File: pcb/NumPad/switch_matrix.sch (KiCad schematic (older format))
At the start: 49 parts, among them SW1 +, SW10 ,, SW11 *, SW12 9, SW13 6, SW14 3, SW15 ., SW16 /, SW17 FN2, SW18 FN1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

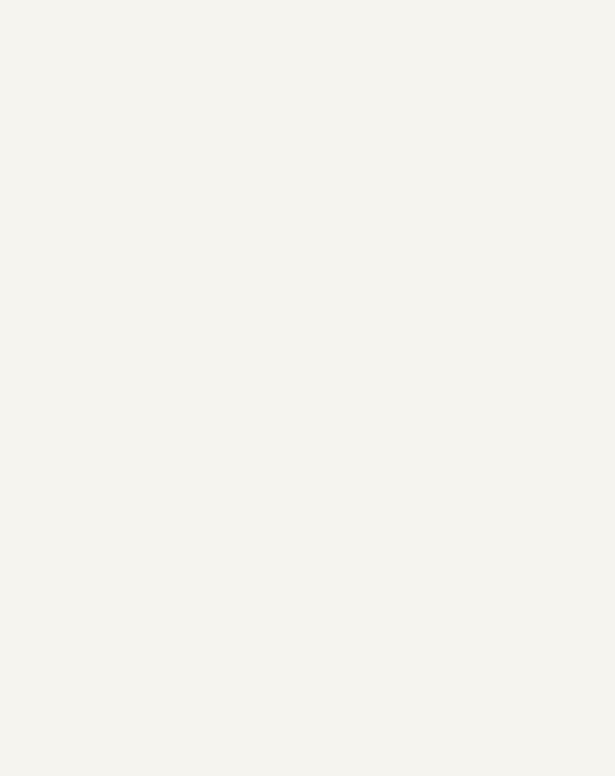
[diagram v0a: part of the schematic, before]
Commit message: started Numpad Layout
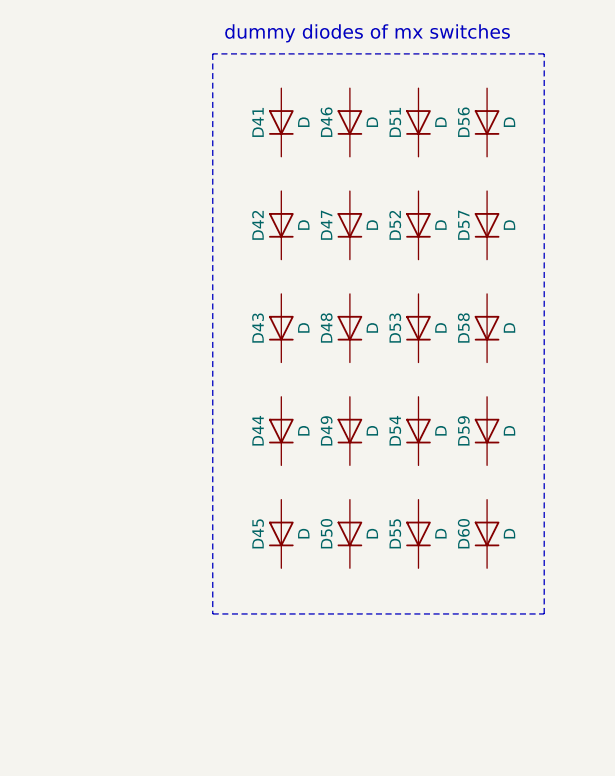
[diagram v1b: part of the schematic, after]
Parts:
- added D41, D42, D43, D44, D45, D46, D47, D48, D49, D50, D51, D52, D53, D54, D55, D56, D57, D58, D59, D60: D, footprints:CHERRY_MX_DIODE, symbol D
- D1, D10, D11, D12, D13, D14, D15, D16, D17, D18, D19, D2, D20, D3, D4, D5, D6, D7, D8, D9: footprint Diodes_SMD:D_SOD-523 -> Diodes_SMD:D_SOD-323_HandSoldering
- SW3: footprint footprints:CHERRY_PCB_150H -> footprints:CHERRY_PCB_100H
- SW4: footprint footprints:CHERRY_PCB_175H -> footprints:CHERRY_PCB_100H
- SW5: footprint footprints:CHERRY_PCB_125H -> footprints:CHERRY_PCB_100H
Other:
- note added: "dummy diodes of mx switches"

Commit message: changes in Numpad
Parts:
- removed D48, D53: D, footprints:CHERRY_MX_DIODE, symbol D
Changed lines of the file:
@@
-$EndComp
-$Comp
-L D D48
-U 1 1 5ABC28EE
-P 11250 5250
-F 0 "D48" H 11250 5350 50  0000 C CNN
-F 1 "D" H 11250 5150 50  0000 C CNN
-F 2 "footprints:CHERRY_MX_DIODE" H 11250 5250 50  0001 C CNN
-F 3 "" H 11250 5250 50  0001 C CNN
-	1    11250 5250
-	0    -1   -1   0
-$EndComp
-$Comp
-L D D53
-U 1 1 5ABC29B7
-P 11550 5250
-F 0 "D53" H 11550 5350 50  0000 C CNN
-F 1 "D" H 11550 5150 50  0000 C CNN
-F 2 "footprints:CHERRY_MX_DIODE" H 11550 5250 50  0001 C CNN
-F 3 "" H 11550 5250 50  0001 C CNN
-	1    11550 5250
-	0    -1   -1   0
 $EndComp
 $Comp
